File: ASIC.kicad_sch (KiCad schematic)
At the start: 124 parts, among them U10 TLV77308PDBVR, U11 TLV77312PDBVR, U13 TS3011, U14 SN74AVC2T45DCUR, U15 25MHz, U6 TLV77312PDBVR, U7 TLV77308PDBVR, U8 25MHz

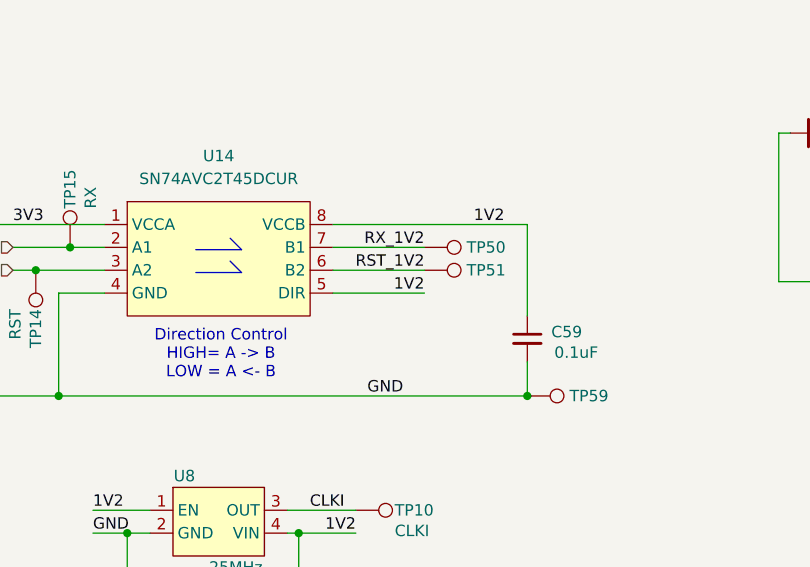
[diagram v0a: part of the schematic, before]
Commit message: fix TPS546 frequency for #4 - fix SN74AVC2T45 level shifter DIR voltage for #2
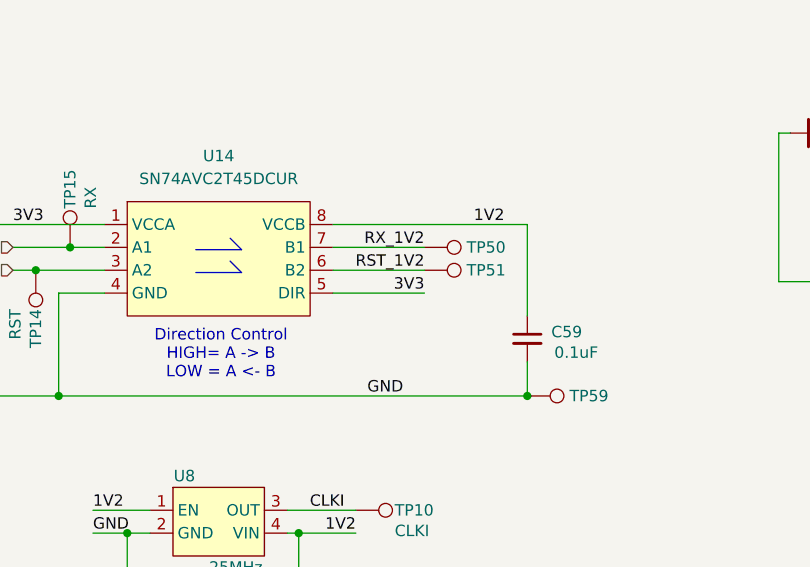
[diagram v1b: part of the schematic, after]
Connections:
- net 1V2: no longer U14.5 (DIR)
- net 3V3: now also U14.5 (DIR)
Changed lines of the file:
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@@
 		(title "bitaxeProto")
 		(date "2026-05-12")
-		(rev "1102xx")
+		(rev "1103xx")
 		(company "bitaxeorg")
 		(comment 1 "OHL v2")
@@
 		)
 	)
-	(label "1V2"
-		(at 137.16 222.25 180)
-		(effects
-			(font
-				(size 1.27 1.27)
-			)
-			(justify right bottom)
-		)
-	)
 	(label "1V2-0"
 		(at 433.07 104.14 0)
@@
 		(effects
 			(font
+				(size 1.27 1.27)
+			)
+			(justify right bottom)
+		)
+	)
+	(label "3V3"
+		(at 137.16 222.25 180)
+		(effects
+			(font

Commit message: add domain voltage sensing for #3 -- just schematic so far
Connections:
- net GND0 renamed DOMAIN_V
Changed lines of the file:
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@@
 	)
 	(junction
+		(at 222.25 165.1)
+		(diameter 0)
+		(color 0 0 0 0)
+	)
+	(junction
 		(at 496.57 101.6)
 		(diameter 0)
@@
 	(wire
 		(pts
+			(xy 222.25 165.1) (xy 222.25 172.72)
+		)
+		(stroke
+			(width 0)
+			(type default)
+		)
+	)
+	(wire
+		(pts
 			(xy 378.46 204.47) (xy 381 204.47)
 		)
@@
 	(wire
 		(pts
+			(xy 218.44 165.1) (xy 222.25 165.1)
+		)
+		(stroke
+			(width 0)
+			(type default)
+		)
+	)
+	(wire
+		(pts
 			(xy 351.79 172.72) (xy 351.79 187.96)
 		)
@@
 	(wire
 		(pts
-			(xy 222.25 149.86) (xy 222.25 172.72)
+			(xy 222.25 149.86) (xy 222.25 165.1)
 		)
 		(stroke
@@
 		(effects
 			(font
+				(size 1.27 1.27)
+			)
+			(justify right)
+		)
+	)
+	(hierarchical_label "DOMAIN_V"
+		(shape output)
+		(at 218.44 165.1 180)
+		(effects
+			(font

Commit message: changed fan connector footprint back to normal. lots of part substitutions for JLCPCB. Mounting hole changes for enclosure
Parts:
- C100, C101, C102, C103, C104, C105, C106, C107, C108, C109, C110, C111, C112, C113, C114, C115, C116, C117, C118, C119, C120, C121, C122, C123, C124, C125, C126, C127, C128, C129, C209, C25, C49, C50, C53, C54, C55, C56, C57, C98, C99: DK 587-5514-1-ND -> (none); Manufacturer (none) -> Samsung Electro-Mechanics; PARTNO EMK105BJ105MV-F -> CL05A105KA5NQNC
- C130, C208, C51, C52, C59, C61, C72, C84, C86, C88, C90, C91, C96: DK 490-10700-1-ND -> (none); LCSC C77020 -> C307331; Manufacturer (none) -> Samsung Electro-Mechanics; PARTNO GRM155R71H104KE14D -> CL05B104KB54PNC
- C131, C79, C85, C87, C89, C92, C94, C97: DK 490-14306-1-ND -> (none); LCSC (none) -> C23733; Manufacturer (none) -> Samsung Electro-Mechanics; PARTNO GRM155R61A475MEAAD -> CL05A475MP5NRNC
- C66, C67, C68, C69, C70, C71, C73, C74, C75, C78, C80, C81, C82, C83, C93, C95: DK 490-18214-1-ND -> (none); LCSC (none) -> C96446; Manufacturer (none) -> Samsung Electro-Mechanics; PARTNO GRM188R61E106KA73D -> CL10A106MA8NRNC
- R25: DK 311-10KJRCT-ND -> (none); Manufacturer (none) -> UNI-ROYAL(Uniroyal Elec); PARTNO RC0402JR-0710KL -> 0402WGF1002TCE
- R26: DK 311-12.0KLRCT-ND -> (none); LCSC (none) -> C25752; Manufacturer (none) -> UNI-ROYAL(Uniroyal Elec); PARTNO RC0402FR-0712KL -> 0402WGF1202TCE
- R71: DK 311-1.00KLRCT-ND -> (none); LCSC (none) -> C11702; Manufacturer (none) -> UNI-ROYAL(Uniroyal Elec); PARTNO RC0402FR-071KL -> 0402WGF1001TCE

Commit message: re-added many missing LCSC part numbers that got lost in translation
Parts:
- R70: LCSC (none) -> C138030
- U10, U7: LCSC (none) -> C51953196
- U11, U6: LCSC (none) -> C30806341
- U13: LCSC (none) -> C20882980
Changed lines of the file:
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@@
 		(pin "2"
 		)
-		(instances
+		    (property "LCSC" "C138030"
+      (at 0 0 0)
+      (effects (font (size 1.27 1.27)) (hide yes))
+    )
+    (instances
 			(project "bitaxeProto"
 				(path "/61fe8d2c-9301-4ad9-8caf-c47acfa835b0/5053a6d5-ae8d-4ae0-9f6e-0d65e80da719"
@@
 		(pin "3"
 		)
-		(instances
+		    (property "LCSC" "C30806341"
+      (at 0 0 0)
+      (effects (font (size 1.27 1.27)) (hide yes))
+    )
+    (instances
 			(project "bitaxeProto"
 				(path "/61fe8d2c-9301-4ad9-8caf-c47acfa835b0/5053a6d5-ae8d-4ae0-9f6e-0d65e80da719"
@@
 		(pin "3"
 		)
-		(instances
+		    (property "LCSC" "C30806341"
+      (at 0 0 0)
+      (effects (font (size 1.27 1.27)) (hide yes))
+    )
+    (instances
 			(project "bitaxeProto"
 				(path "/61fe8d2c-9301-4ad9-8caf-c47acfa835b0/5053a6d5-ae8d-4ae0-9f6e-0d65e80da719"
@@
 		(pin "3"
 		)
-		(instances
+		    (property "LCSC" "C51953196"
+      (at 0 0 0)
+      (effects (font (size 1.27 1.27)) (hide yes))
+    )
+    (instances
 			(project "bitaxeProto"
 				(path "/61fe8d2c-9301-4ad9-8caf-c47acfa835b0/5053a6d5-ae8d-4ae0-9f6e-0d65e80da719"
@@
 		(pin "2"
 		)
-		(instances
+		    (property "LCSC" "C20882980"
+      (at 0 0 0)
+      (effects (font (size 1.27 1.27)) (hide yes))
+    )
+    (instances
 			(project "bitaxeProto"
 				(path "/61fe8d2c-9301-4ad9-8caf-c47acfa835b0/5053a6d5-ae8d-4ae0-9f6e-0d65e80da719"
@@
 		(pin "3"
 		)
-		(instances
+		    (property "LCSC" "C51953196"
+      (at 0 0 0)
+      (effects (font (size 1.27 1.27)) (hide yes))
+    )
+    (instances
 			(project "bitaxeProto"
 				(path "/61fe8d2c-9301-4ad9-8caf-c47acfa835b0/5053a6d5-ae8d-4ae0-9f6e-0d65e80da719"

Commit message: DRC fixes. added filled via notes. power track tweaking. switched fan connecter back to normal (again)
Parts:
- removed TP11: CLKI, bitaxe:TestPoint_Pad_D1.0mm, symbol Connector:TestPoint
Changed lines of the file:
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@@
 			)
 		)
+		(property "LCSC" "C138030"
+			(at 0 0 0)
+			(hide yes)
+			(show_name no)
+			(do_not_autoplace no)
+			(effects
+				(font
+					(size 1.27 1.27)
+				)
+			)
+		)
 		(pin "1"
 		)
 		(pin "2"
 		)
-		    (property "LCSC" "C138030"
-      (at 0 0 0)
-      (effects (font (size 1.27 1.27)) (hide yes))
-    )
-    (instances
+		(instances
 			(project "bitaxeProto"
 				(path "/61fe8d2c-9301-4ad9-8caf-c47acfa835b0/5053a6d5-ae8d-4ae0-9f6e-0d65e80da719"
@@
 			)
 		)
+		(property "LCSC" "C30806341"
+			(at 0 0 0)
+			(hide yes)
+			(show_name no)
+			(do_not_autoplace no)
+			(effects
+				(font
+					(size 1.27 1.27)
+				)
+			)
+		)
 		(pin "1"
 		)
@@
 		(pin "3"
 		)
-		    (property "LCSC" "C30806341"
-      (at 0 0 0)
-      (effects (font (size 1.27 1.27)) (hide yes))
-    )
-    (instances
+		(instances
 			(project "bitaxeProto"
 				(path "/61fe8d2c-9301-4ad9-8caf-c47acfa835b0/5053a6d5-ae8d-4ae0-9f6e-0d65e80da719"
@@
 	)
 	(symbol
-		(lib_id "Connector:TestPoint")
-		(at 433.07 101.6 90)
-		(mirror x)
-		(unit 1)
-		(body_style 1)
-		(exclude_from_sim no)
-		(in_bom no)
-		(on_board yes)
-		(in_pos_files yes)
-		(dnp no)
-		(property "Reference" "TP11"
-			(at 428.752 101.6 90)
-			(show_name no)
-			(do_not_autoplace no)
-			(effects
-				(font
-					(size 1.27 1.27)
-				)
-				(justify left)
-			)
-		)
-		(property "Value" "CLKI"
-			(at 428.752 103.886 90)
-			(show_name no)
-			(do_not_autoplace no)
-			(effects
-				(font
-					(size 1.27 1.27)
-				)
-				(justify left)
-			)
-		)
-		(property "Footprint" "bitaxe:TestPoint_Pad_D1.0mm"
-			(at 433.07 106.68 0)
-			(hide yes)
-			(show_name no)
-			(do_not_autoplace no)
-			(effects
-				(font
-					(size 1.27 1.27)
-				)
-			)
-		)
-		(property "Datasheet" ""
-			(at 433.07 106.68 0)
-			(hide yes)
-			(show_name no)
-			(do_not_autoplace no)
-			(effects
-				(font
-					(size 1.27 1.27)
-				)
-			)
-		)
-		(property "Description" "test point"
-			(at 433.07 101.6 0)
-			(hide yes)
-			(show_name no)
-			(do_not_autoplace no)
-			(effects
-				(font
-					(size 1.27 1.27)
-				)
-			)
-		)
-		(property "Sim.Device" ""
-			(at 433.07 101.6 90)
-			(hide yes)
-			(show_name no)
-			(do_not_autoplace no)
-			(effects
-				(font
-					(size 1.27 1.27)
-				)
-			)
-		)
-		(property "Sim.Pins" ""
-			(at 433.07 101.6 90)
-			(hide yes)
-			(show_name no)
-			(do_not_autoplace no)
-			(effects
-				(font
-					(size 1.27 1.27)
-				)
-			)
-		)
-		(pin "1"
-		)
-		(instances
-			(project "bitaxeProto"
-				(path "/61fe8d2c-9301-4ad9-8caf-c47acfa835b0/5053a6d5-ae8d-4ae0-9f6e-0d65e80da719"
-					(reference "TP11")
-					(unit 1)
-				)
-			)
-		)
-	)
-	(symbol
 		(lib_id "Device:C_Small")
 		(at 410.21 138.43 180)
@@
 			)
 		)
+		(property "LCSC" "C30806341"
+			(at 0 0 0)
+			(hide yes)
+			(show_name no)
+			(do_not_autoplace no)
+			(effects
+				(font
+					(size 1.27 1.27)
+				)
+			)
+		)
 		(pin "1"
 		)
@@
 		(pin "3"
 		)
-		    (property "LCSC" "C30806341"
-      (at 0 0 0)
-      (effects (font (size 1.27 1.27)) (hide yes))
-    )
-    (instances
+		(instances
 			(project "bitaxeProto"
 				(path "/61fe8d2c-9301-4ad9-8caf-c47acfa835b0/5053a6d5-ae8d-4ae0-9f6e-0d65e80da719"
@@
 			)
 		)
+		(property "LCSC" "C51953196"
+			(at 0 0 0)
+			(hide yes)
+			(show_name no)
+			(do_not_autoplace no)
+			(effects
+				(font
+					(size 1.27 1.27)
+				)
+			)
+		)
 		(pin "1"
 		)
@@
 		(pin "3"
 		)
-		    (property "LCSC" "C51953196"
-      (at 0 0 0)
-      (effects (font (size 1.27 1.27)) (hide yes))
-    )
-    (instances
+		(instances
 			(project "bitaxeProto"
 				(path "/61fe8d2c-9301-4ad9-8caf-c47acfa835b0/5053a6d5-ae8d-4ae0-9f6e-0d65e80da719"
@@
 			)
 		)
+		(property "LCSC" "C20882980"
+			(at 0 0 0)
+			(hide yes)
+			(show_name no)
+			(do_not_autoplace no)
+			(effects
+				(font
+					(size 1.27 1.27)
+				)
+			)
+		)
 		(pin "4"
 		)
@@
 		(pin "2"
 		)
-		    (property "LCSC" "C20882980"
-      (at 0 0 0)
-      (effects (font (size 1.27 1.27)) (hide yes))
-    )
-    (instances
+		(instances
 			(project "bitaxeProto"
 				(path "/61fe8d2c-9301-4ad9-8caf-c47acfa835b0/5053a6d5-ae8d-4ae0-9f6e-0d65e80da719"
@@
 			)
 		)
+		(property "LCSC" "C51953196"
+			(at 0 0 0)
+			(hide yes)
+			(show_name no)
+			(do_not_autoplace no)
+			(effects
+				(font
+					(size 1.27 1.27)
+				)
+			)
+		)
 		(pin "1"
 		)
@@
 		(pin "3"
 		)
-		    (property "LCSC" "C51953196"
-      (at 0 0 0)
-      (effects (font (size 1.27 1.27)) (hide yes))
-    )
-    (instances
+		(instances
 			(project "bitaxeProto"
 				(path "/61fe8d2c-9301-4ad9-8caf-c47acfa835b0/5053a6d5-ae8d-4ae0-9f6e-0d65e80da719"

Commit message: switch to cheaper USB-C connector
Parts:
- U10, U7: DK 296-TLV77308PDBVRCT-ND -> (none); PARTNO TLV77308PDBVR -> LW8108A23E
- U13: DK 497-11991-1-ND -> (none); PARTNO TS3011ILT -> MX7219T
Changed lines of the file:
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@@
 			)
 		)
-		(property "DK" "296-TLV77308PDBVRCT-ND"
+		(property "DK" ""
 			(at 506.73 104.14 0)
 			(hide yes)
@@
 			)
 		)
-		(property "PARTNO" "TLV77308PDBVR"
+		(property "PARTNO" "LW8108A23E"
 			(at 506.73 104.14 0)
 			(hide yes)
@@
 			)
 		)
-		(property "PARTNO" "TS3011ILT"
+		(property "PARTNO" "MX7219T"
 			(at 87.376 142.748 0)
 			(hide yes)
@@
 			)
 		)
-		(property "DK" "497-11991-1-ND"
+		(property "DK" ""
 			(at 86.614 145.034 0)
 			(hide yes)
@@
 			)
 		)
-		(property "DK" "296-TLV77308PDBVRCT-ND"
+		(property "DK" ""
 			(at 506.73 217.17 0)
 			(hide yes)
@@
 			)
 		)
-		(property "PARTNO" "TLV77308PDBVR"
+		(property "PARTNO" "LW8108A23E"
 			(at 506.73 217.17 0)
 			(hide yes)

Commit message: updated part values for 3 components to match actual
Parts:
- U10, U7: value TLV77308PDBVR -> LW8108A23E
- U13: value TS3011 -> MX7219T
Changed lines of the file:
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@@
 			)
 		)
-		(property "Value" "TLV77308PDBVR"
+		(property "Value" "LW8108A23E"
 			(at 506.73 97.79 0)
 			(show_name no)
@@
 			)
 		)
-		(property "Value" "TS3011"
+		(property "Value" "MX7219T"
 			(at 93.726 121.666 0)
 			(show_name no)
@@
 			)
 		)
-		(property "Value" "TLV77308PDBVR"
+		(property "Value" "LW8108A23E"
 			(at 506.73 210.82 0)
 			(show_name no)

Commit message: updated part attributes for JLCPCB Fabrication Toolkit
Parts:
- U10, U11, U13, U6, U7: FT Rotation Offset (none) -> -90
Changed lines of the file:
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@@
 			)
 		)
+		(property "FT Rotation Offset" "-90"
+			(at 506.73 243.84 0)
+			(hide yes)
+			(show_name no)
+			(do_not_autoplace no)
+			(effects
+				(font
+					(size 1.27 1.27)
+				)
+			)
+		)
 		(pin "1"
 		)
@@
 			)
 		)
+		(property "FT Rotation Offset" "-90"
+			(at 506.73 130.81 0)
+			(hide yes)
+			(show_name no)
+			(do_not_autoplace no)
+			(effects
+				(font
+					(size 1.27 1.27)
+				)
+			)
+		)
 		(pin "1"
 		)
@@
 			)
 		)
+		(property "FT Rotation Offset" "-90"
+			(at 506.73 104.14 0)
+			(hide yes)
+			(show_name no)
+			(do_not_autoplace no)
+			(effects
+				(font
+					(size 1.27 1.27)
+				)
+			)
+		)
 		(pin "1"
 		)
@@
 			)
 		)
+		(property "FT Rotation Offset" "-90"
+			(at 97.79 125.73 0)
+			(hide yes)
+			(show_name no)
+			(do_not_autoplace no)
+			(effects
+				(font
+					(size 1.27 1.27)
+				)
+			)
+		)
 		(pin "4"
 		)
@@
 			(hide yes)
 			(show_name no)
+			(do_not_autoplace no)
+			(effects
+				(font
+					(size 1.27 1.27)
+				)
+			)
+		)
+		(property "FT Rotation Offset" "-90"
+			(at 506.73 217.17 0)
+			(hide yes)
+			(show_name no)
